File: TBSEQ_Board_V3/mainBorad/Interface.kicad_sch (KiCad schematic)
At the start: 49 parts, among them IC12 4066, IC2 NJM2125F-TE1, J2 Conn_01x05_Pin, J7 Conn_01x03_Pin, J8 Conn_01x02_Pin, J9 Conn_01x01_Pin, Q29 NPN, Q30 NPN, Q35 NPN, Q36 PNP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

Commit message: BoardV3
ERCチェック済
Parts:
- added unit 5 of IC12
- IC12: footprint Package_DIP:DIP-14_W7.62mm -> Package_DIP:DIP-14_W7.62mm_LongPads
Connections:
- net A+12V: now also IC12.14 (VDD)
- net GNDA: now also IC12.7 (VSS)
- net at D28.2 (A), VR6.2 (WIPER), VR6.3 (CW): now also IC12.11; no longer IC12.10
- net at R138.1, VR6.1 (CCW): now also IC12.10; no longer IC12.11

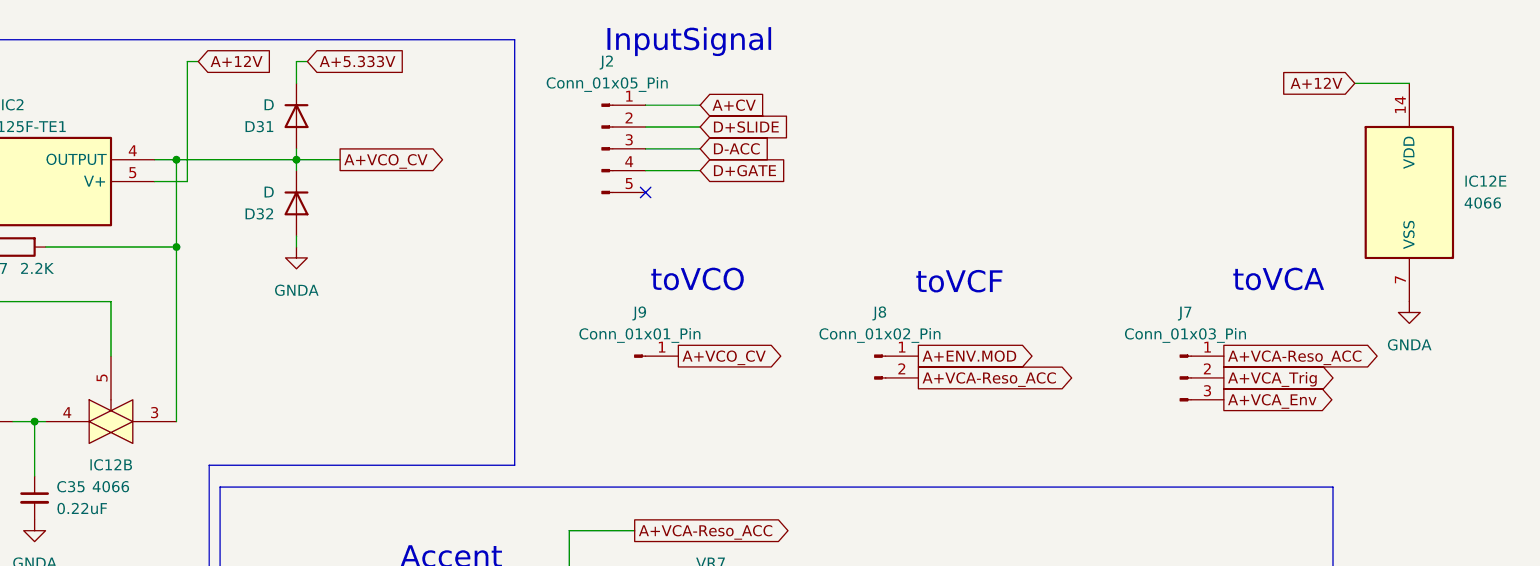
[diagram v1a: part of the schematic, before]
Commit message: V3Board
DualTr フットプリント変更
配線ミス修正
TEMPO削除⇒PanelBoardに移動
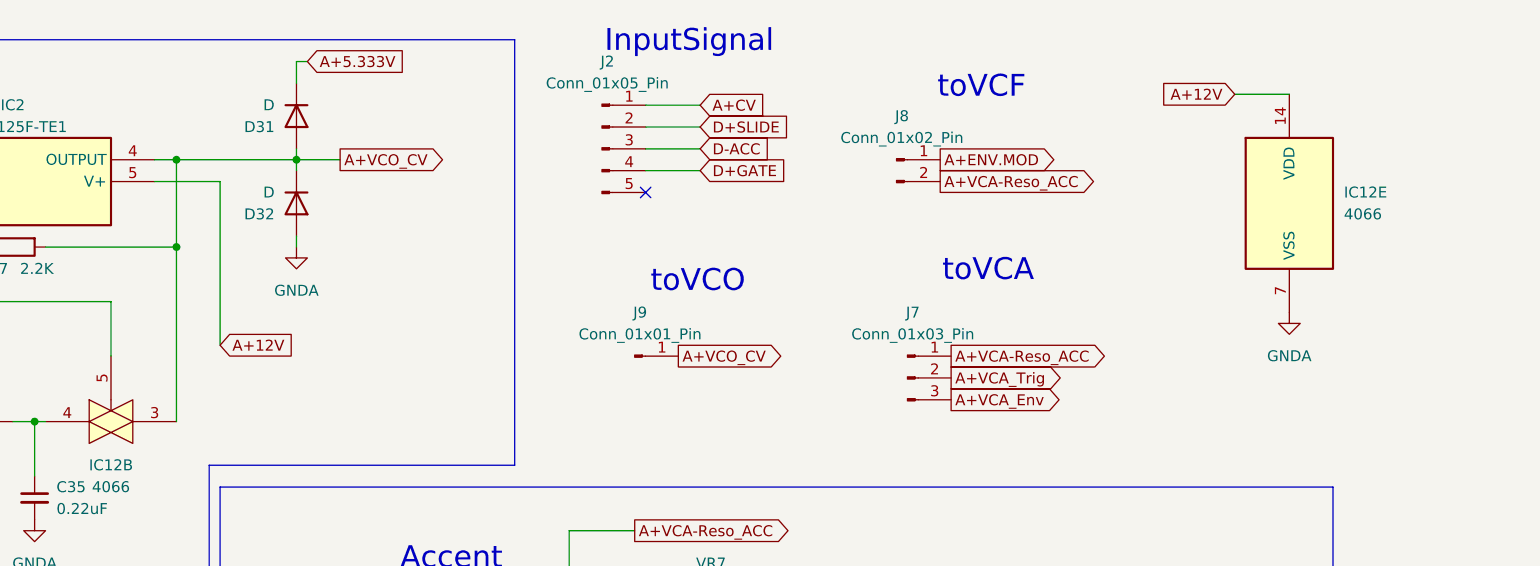
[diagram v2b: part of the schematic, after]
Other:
- moved on the sheet: IC12E, J7, J8
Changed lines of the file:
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@@
 	(wire
 		(pts
-			(xy 127 17.78) (xy 127 31.75)
+			(xy 130.81 50.8) (xy 130.81 31.75)
 		)
 		(stroke
@@
 	(wire
 		(pts
-			(xy 127 31.75) (xy 123.19 31.75)
+			(xy 130.81 31.75) (xy 123.19 31.75)
 		)
 		(stroke
@@
 	(wire
 		(pts
-			(xy 128.27 17.78) (xy 127 17.78)
-		)
-		(stroke
-			(width 0)
-			(type default)
-		)
-	)
-	(wire
-		(pts
 			(xy 62.23 128.27) (xy 62.23 132.08)
 		)
@@
 	(wire
 		(pts
-			(xy 262.89 20.32) (xy 269.24 20.32)
+			(xy 248.92 21.59) (xy 255.27 21.59)
 		)
 		(stroke
@@
 	(text "toVCF"
 		(exclude_from_sim no)
-		(at 216.916 43.688 0)
+		(at 219.456 20.828 0)
 		(effects
 			(font
@@
 	(text "toVCA"
 		(exclude_from_sim no)
-		(at 254 43.434 0)
+		(at 220.218 42.164 0)
 		(effects
 			(font
@@
 	(global_label "A+ENV.MOD"
 		(shape output)
-		(at 212.09 52.07 0)
+		(at 214.63 29.21 0)
 		(fields_autoplaced yes)
 		(effects
@@
 		)
 		(property "Intersheetrefs" "${INTERSHEET_REFS}"
-			(at 230.3153 52.07 0)
+			(at 232.8553 29.21 0)
 			(effects
 				(font
@@
 	(global_label "A+VCA-Reso_ACC"
 		(shape output)
-		(at 247.65 52.07 0)
+		(at 215.9 52.07 0)
 		(fields_autoplaced yes)
 		(effects
@@
 		)
 		(property "Intersheetrefs" "${INTERSHEET_REFS}"
-			(at 265.8753 52.07 0)
+			(at 234.1253 52.07 0)
 			(effects
 				(font
@@
 	(global_label "A+12V"
 		(shape input)
-		(at 262.89 20.32 180)
+		(at 248.92 21.59 180)
 		(fields_autoplaced yes)
 		(effects
@@
 		)
 		(property "Intersheetrefs" "${INTERSHEET_REFS}"
-			(at 253.7362 20.32 0)
+			(at 239.7662 21.59 0)
 			(effects
 				(font
@@
 	(global_label "A+VCA_Trig"
 		(shape output)
-		(at 247.65 54.61 0)
+		(at 215.9 54.61 0)
 		(fields_autoplaced yes)
 		(effects
@@
 		)
 		(property "Intersheetrefs" "${INTERSHEET_REFS}"
-			(at 257.9528 54.61 0)
+			(at 226.2028 54.61 0)
 			(effects
 				(font
@@
 	(global_label "A+VCA-Reso_ACC"
 		(shape output)
-		(at 212.09 54.61 0)
+		(at 214.63 31.75 0)
 		(fields_autoplaced yes)
 		(effects
@@
 		)
 		(property "Intersheetrefs" "${INTERSHEET_REFS}"
-			(at 230.3153 54.61 0)
+			(at 232.8553 31.75 0)
 			(effects
 				(font
@@
 	(global_label "A+VCA_Env"
 		(shape output)
-		(at 247.65 57.15 0)
+		(at 215.9 57.15 0)
 		(fields_autoplaced yes)
 		(effects
@@
 		)
 		(property "Intersheetrefs" "${INTERSHEET_REFS}"
-			(at 260.9766 57.15 0)
+			(at 229.2266 57.15 0)
 			(effects
 				(font
@@
 	(global_label "A+12V"
 		(shape input)
-		(at 128.27 17.78 0)
+		(at 130.81 50.8 0)
 		(fields_autoplaced yes)
 		(effects
@@
 		)
 		(property "Intersheetrefs" "${INTERSHEET_REFS}"
-			(at 140.4476 17.78 0)
+			(at 142.9876 50.8 0)
 			(effects
 				(font
@@
 	(symbol
 		(lib_id "power:GNDA")
-		(at 269.24 45.72 0)
+		(at 255.27 46.99 0)
 		(unit 1)
 		(exclude_from_sim no)
@@
 		(fields_autoplaced yes)
 		(property "Reference" "#PWR046"
-			(at 269.24 52.07 0)
+			(at 255.27 53.34 0)
 			(effects
 				(font
@@
 		)
 		(property "Value" "GNDA"
-			(at 269.24 50.8 0)
+			(at 255.27 52.07 0)
 			(effects
 				(font
@@
 		)
 		(property "Footprint" ""
-			(at 269.24 45.72 0)
+			(at 255.27 46.99 0)
 			(effects
 				(font
@@
 		)
 		(property "Datasheet" ""
-			(at 269.24 45.72 0)
+			(at 255.27 46.99 0)
 			(effects
 				(font
@@
 		)
 		(property "Description" "Power symbol creates a global label with name \"GNDA\" , analog ground"
-			(at 269.24 45.72 0)
+			(at 255.27 46.99 0)
 			(effects
 				(font
@@
 	(symbol
 		(lib_id "4xxx:4066")
-		(at 269.24 33.02 0)
+		(at 255.27 34.29 0)
 		(unit 5)
 		(exclude_from_sim no)
@@
 		(fields_autoplaced yes)
 		(property "Reference" "IC12"
-			(at 275.59 31.7499 0)
+			(at 261.62 33.0199 0)
 			(effects
 				(font
@@
 		)
 		(property "Value" "4066"
-			(at 275.59 34.2899 0)
+			(at 261.62 35.5599 0)
 			(effects
 				(font
@@
 		)
 		(property "Footprint" "Package_DIP:DIP-14_W7.62mm_LongPads"
-			(at 269.24 33.02 0)
+			(at 255.27 34.29 0)
 			(effects
 				(font
@@
 		)
 		(property "Datasheet" "http://www.ti.com/lit/ds/symlink/cd4066b.pdf"
-			(at 269.24 33.02 0)
+			(at 255.27 34.29 0)
 			(effects
 				(font
@@
 		)
 		(property "Description" "Quad Analog Switches"
-			(at 269.24 33.02 0)
+			(at 255.27 34.29 0)
 			(effects
 				(font
@@
 	(symbol
 		(lib_id "Connector:Conn_01x03_Pin")
-		(at 242.57 54.61 0)
+		(at 210.82 54.61 0)
 		(unit 1)
 		(exclude_from_sim no)
@@
 		(fields_autoplaced yes)
 		(property "Reference" "J7"
-			(at 243.205 46.99 0)
+			(at 211.455 46.99 0)
 			(effects
 				(font
@@
 		)
 		(property "Value" "Conn_01x03_Pin"
-			(at 243.205 49.53 0)
+			(at 211.455 49.53 0)
 			(effects
 				(font
@@
 		)
 		(property "Footprint" "Connector_PinHeader_2.54mm:PinHeader_1x03_P2.54mm_Vertical"
-			(at 242.57 54.61 0)
+			(at 210.82 54.61 0)
 			(effects
 				(font
@@
 		)
 		(property "Datasheet" "~"
-			(at 242.57 54.61 0)
+			(at 210.82 54.61 0)
 			(effects
 				(font
@@
 		)
 		(property "Description" "Generic connector, single row, 01x03, script generated"
-			(at 242.57 54.61 0)
+			(at 210.82 54.61 0)
 			(effects
 				(font
@@
 	(symbol
 		(lib_id "Connector:Conn_01x02_Pin")
-		(at 207.01 52.07 0)
+		(at 209.55 29.21 0)
 		(unit 1)
 		(exclude_from_sim no)
@@
 		(fields_autoplaced yes)
 		(property "Reference" "J8"
-			(at 207.645 46.99 0)
+			(at 210.185 24.13 0)
 			(effects
 				(font
@@
 		)
 		(property "Value" "Conn_01x02_Pin"
-			(at 207.645 49.53 0)
+			(at 210.185 26.67 0)
 			(effects
 				(font
@@
 		)
 		(property "Footprint" "Connector_PinHeader_2.54mm:PinHeader_1x02_P2.54mm_Vertical"
-			(at 207.01 52.07 0)
+			(at 209.55 29.21 0)
 			(effects
 				(font
@@
 		)
 		(property "Datasheet" "~"
-			(at 207.01 52.07 0)
+			(at 209.55 29.21 0)
 			(effects
 				(font
@@
 		)
 		(property "Description" "Generic connector, single row, 01x02, script generated"
-			(at 207.01 52.07 0)
+			(at 209.55 29.21 0)
 			(effects
 				(font

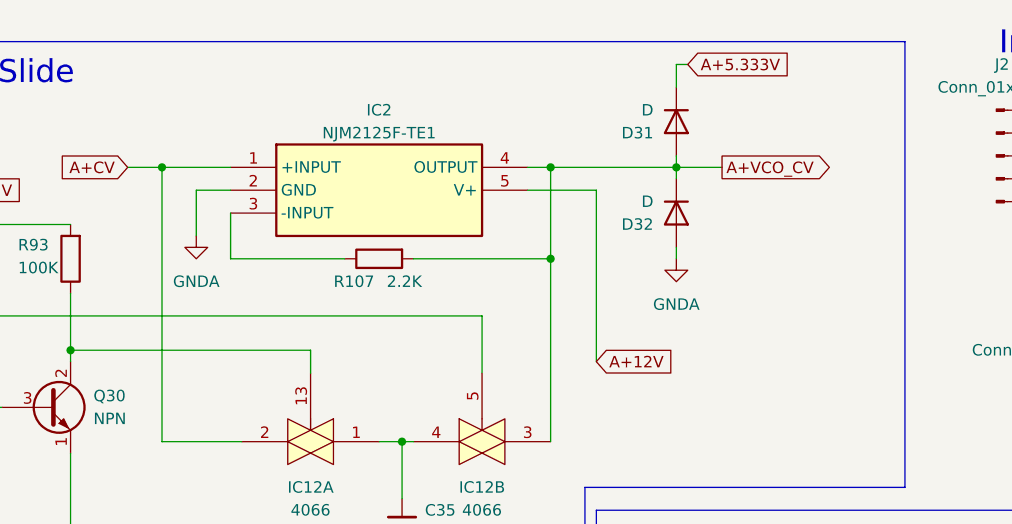
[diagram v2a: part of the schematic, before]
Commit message: V3Board
opamp Dip8に対応
部品配置
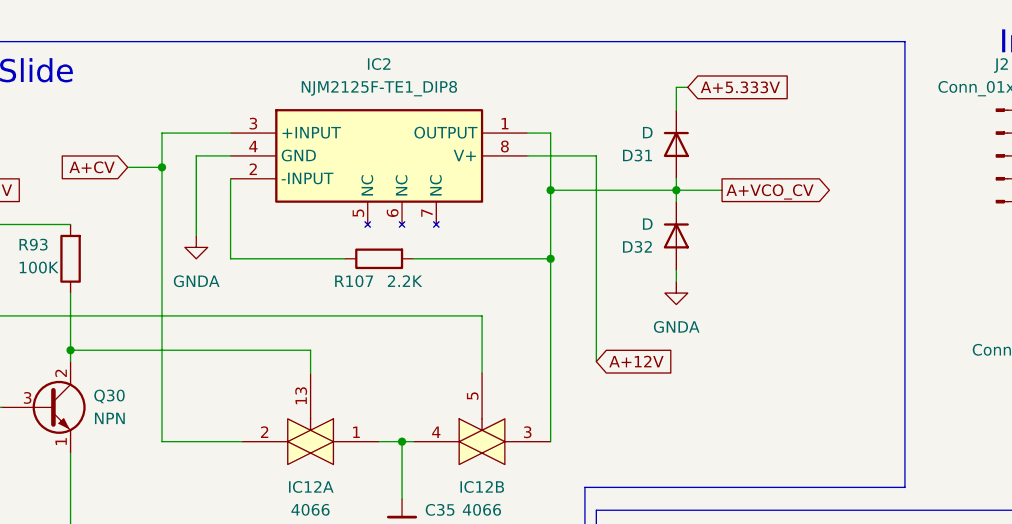
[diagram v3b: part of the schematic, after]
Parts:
- removed IC2: NJM2125F-TE1, SOT95P280X130-5N, symbol SamacSys_Parts:NJM2125F-TE1
- added IC2: NJM2125F-TE1_DIP8, SamacSys_Parts:NJM2125F-SOT95&DIP8, symbol SamacSys_Parts:NJM2125F-TE1_DIP-8
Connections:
- net A+12V: now also IC2.8 (V+)
- net A+CV: now also IC2.3 (+INPUT)
- net A+VCO_CV: now also IC2.1 (OUTPUT)
- net GNDA: now also IC2.4 (GND)
- net at R107.1: now also IC2.2 (-INPUT)
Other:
- moved on the sheet: D31, D32

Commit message: V3Board
アートワーク中
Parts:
- removed IC2: NJM2125F-TE1_DIP8, SamacSys_Parts:NJM2125F-SOT95&DIP8, symbol SamacSys_Parts:NJM2125F-TE1_DIP-8
- removed J2: Conn_01x05_Pin, Connector_PinHeader_2.54mm:PinHeader_1x05_P2.54mm_Vertical, symbol Connector:Conn_01x05_Pin
- added IC2: NJM2125F-TE1, SamacSys_Parts:SOT95P280X130-5N, symbol SamacSys_Parts:NJM2125F-TE1
- Q29, Q30, Q35, Q36, Q37, Q38, Q39, Q40, Q41: footprint Package_TO_SOT_THT:TO-92_Inline -> Package_TO_SOT_THT:TO-92_HandSolder
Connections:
- net A+12V: now also IC2.5 (V+)
- net A+CV: now also IC2.1 (+INPUT)
- net A+VCO_CV: now also IC2.4 (OUTPUT)
- net GNDA: now also IC2.2 (GND)
- net at R107.1: now also IC2.3 (-INPUT)
- no-connect marks 3 -> 2
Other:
- note removed: "InputSignal"
- moved on the sheet: R107

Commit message: V3Board
GNDパターン塗り済
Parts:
- removed J9: Conn_01x01_Pin, Connector_PinHeader_2.54mm:PinHeader_1x01_P2.54mm_Vertical, symbol Connector:Conn_01x01_Pin
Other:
- note removed: "toVCO"
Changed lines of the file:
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@@
 		)
 	)
-	(text "toVCO"
-		(exclude_from_sim no)
-		(at 186.436 43.434 0)
-		(effects
-			(font
-				(size 2.54 2.54)
-			)
-		)
-	)
 	(text "G"
 		(exclude_from_sim no)
@@
 		)
 	)
-	(global_label "A+VCO_CV"
-		(shape output)
-		(at 184.15 52.07 0)
-		(fields_autoplaced yes)
-		(effects
-			(font
-				(size 1.27 1.27)
-			)
-			(justify left)
-		)
-		(property "Intersheetrefs" "${INTERSHEET_REFS}"
-			(at 196.8115 52.07 0)
-			(effects
-				(font
-					(size 1.27 1.27)
-				)
-				(justify left)
-				(hide yes)
-			)
-		)
-	)
 	(global_label "A+VCA_Trig"
 		(shape output)
@@
 					(unit 1)
 				)
-			)
-		)
-	)
-	(symbol
-		(lib_id "Connector:Conn_01x01_Pin")
-		(at 179.07 52.07 0)
-		(unit 1)
-		(exclude_from_sim no)
-		(in_bom yes)
-		(on_board yes)
-		(dnp no)
-		(fields_autoplaced yes)
-		(property "Reference" "J9"
-			(at 179.705 46.99 0)
-			(effects
-				(font
-					(size 1.27 1.27)
-				)
-			)
-		)
-		(property "Value" "Conn_01x01_Pin"
-			(at 179.705 49.53 0)
-			(effects
-				(font
-					(size 1.27 1.27)
-				)
-			)
-		)
-		(property "Footprint" "Connector_PinHeader_2.54mm:PinHeader_1x01_P2.54mm_Vertical"
-			(at 179.07 52.07 0)
-			(effects
-				(font
-					(size 1.27 1.27)
-				)
-				(hide yes)
-			)
-		)
-		(property "Datasheet" "~"
-			(at 179.07 52.07 0)
-			(effects
-				(font
-					(size 1.27 1.27)
-				)
-				(hide yes)
-			)
-		)
-		(property "Description" "Generic connector, single row, 01x01, script generated"
-			(at 179.07 52.07 0)
-			(effects
-				(font
-					(size 1.27 1.27)
-				)
-				(hide yes)
-			)
-		)
-		(property "Sim.Library" ""
-			(at 179.07 52.07 0)
-			(effects
-				(font
-					(size 1.27 1.27)
-				)
-				(hide yes)
-			)
-		)
-		(property "Sim.Name" ""
-			(at 179.07 52.07 0)
-			(effects
-				(font
-					(size 1.27 1.27)
-				)
-				(hide yes)
-			)
-		)
-		(pin "1"
-		)
-		(instances
-			(project "analog_separate"
-				(path "/83af791a-9776-40a7-82ad-9528ff7474b8/89dc079b-4bec-462d-b3d4-975f87bf224f"
-					(reference "J9")
-					(unit 1)
-				)
-			)
-			(project "analog_separate"
-				(path "/96522794-a695-4466-86ba-4264882708e5/f3375c55-8148-47b4-9d07-6863d0fa6703"
-					(reference "J9")
-					(unit 1)
-				)

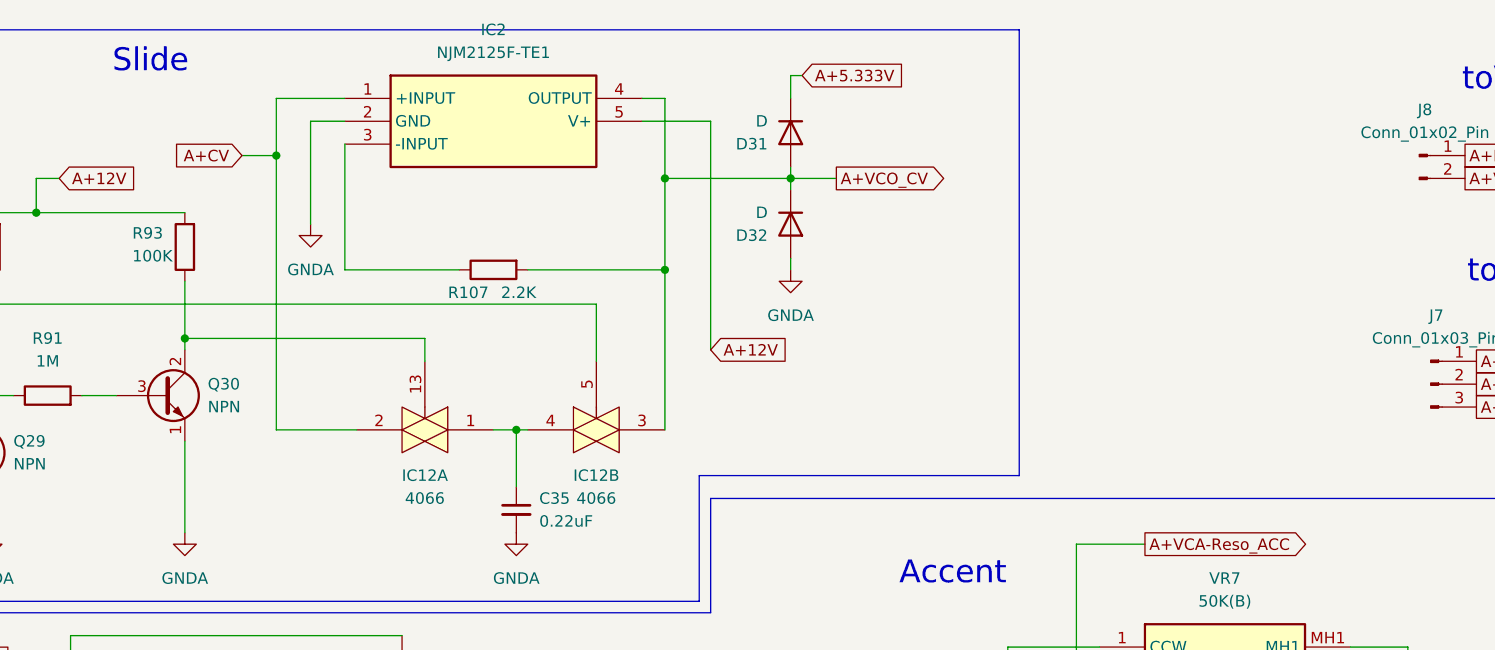
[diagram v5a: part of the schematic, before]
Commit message: V3Board
DualTr OPAmp やはりDIPに変更してオートルーター前に戻す
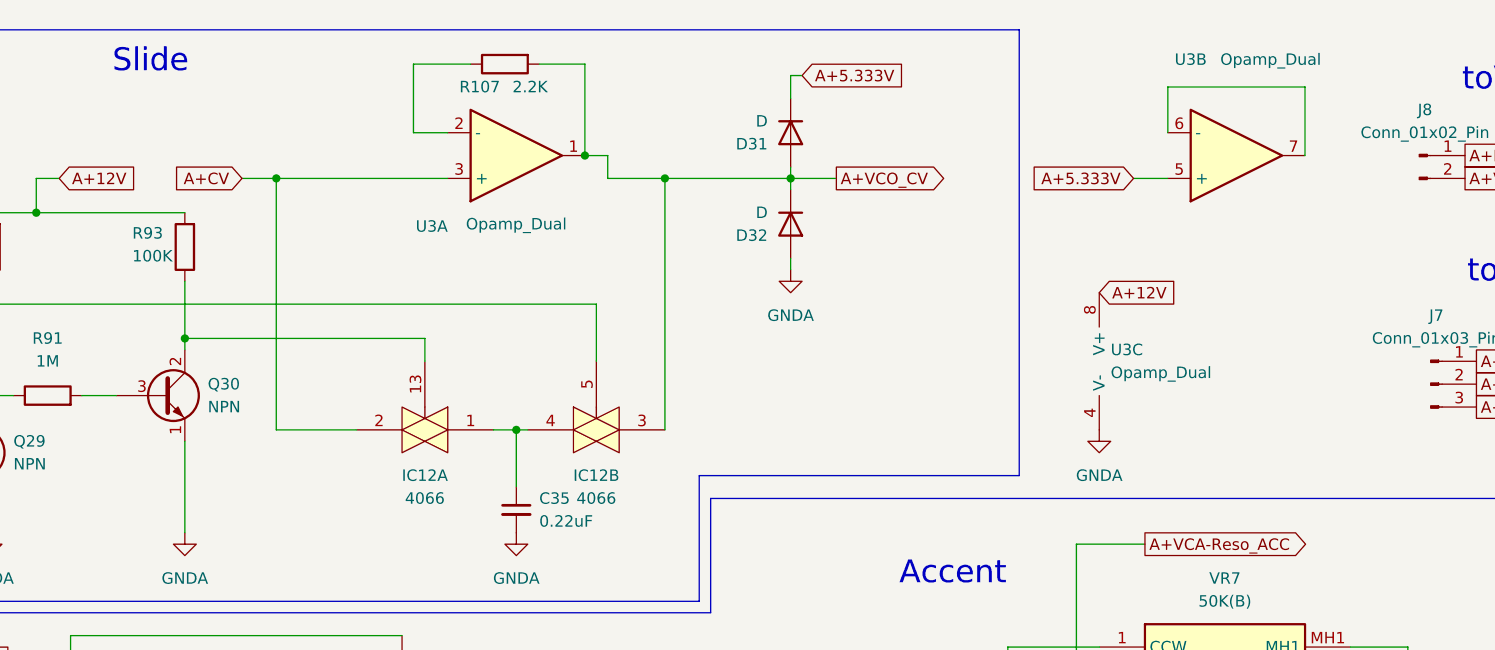
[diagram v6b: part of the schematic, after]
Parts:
- removed IC2: NJM2125F-TE1, SamacSys_Parts:SOT95P280X130-5N, symbol SamacSys_Parts:NJM2125F-TE1
- added U3: Opamp_Dual, Package_DIP:DIP-8_W7.62mm_LongPads, symbol Device:Opamp_Dual
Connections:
- net A+12V: now also U3.8 (V+)
- net A+5.333V: now also U3.5 (+)
- net A+CV: now also U3.3 (+)
- net A+VCO_CV: now also U3.1
- net GNDA: now also U3.4 (V-)
- net at R107.1: now also U3.2 (-)
- new net: U3.6 (-), U3.7
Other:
- moved on the sheet: R107
